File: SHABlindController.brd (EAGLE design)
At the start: 123 x 24 mm, 37 parts, among them IC1 SPARKCORE, IC2 RAC02-05SC, IC3 RXB1SIL, Q1 2N7002, Q2 2N7002

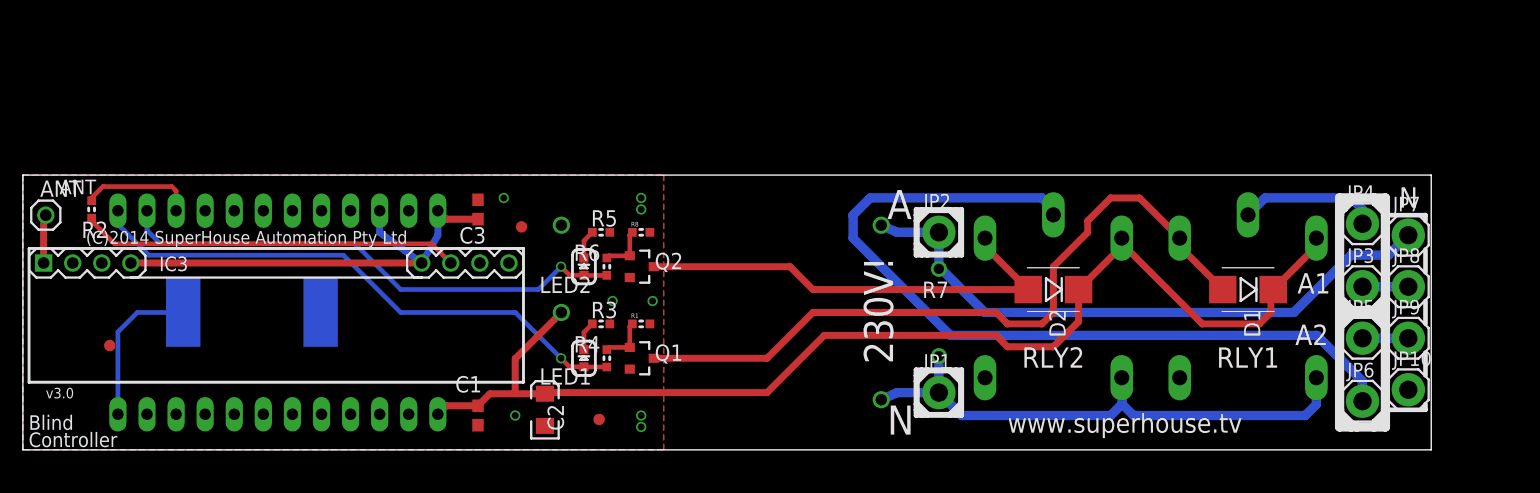
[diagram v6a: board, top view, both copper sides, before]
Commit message: v4.0 release: improved 433MHz rx footprint, added PTH option for piezo
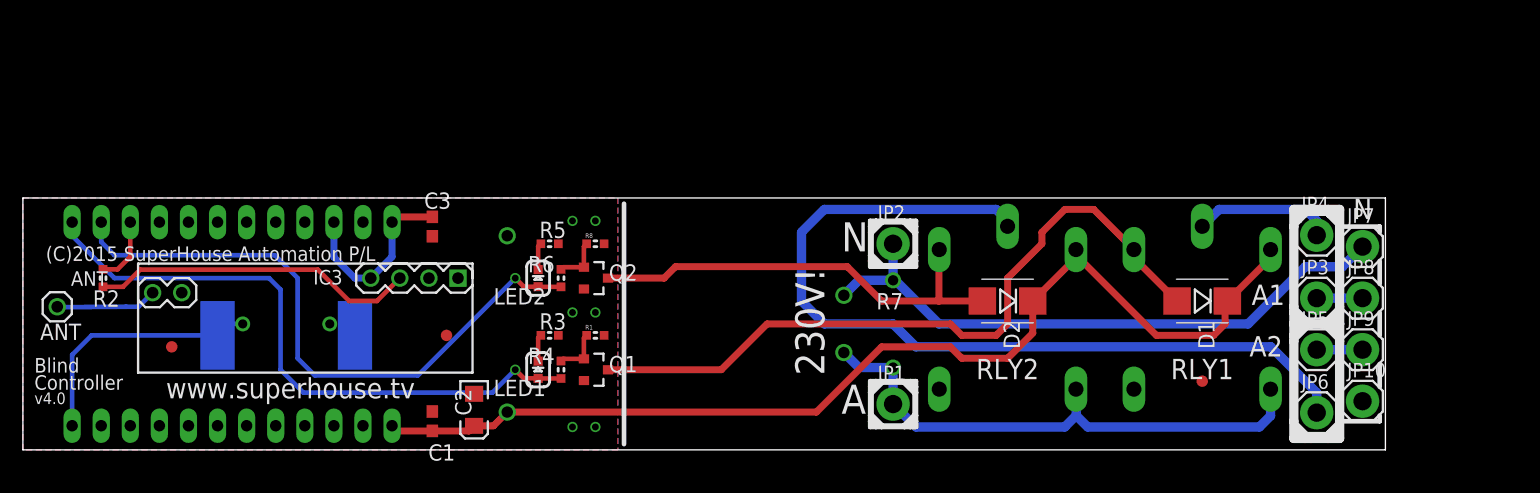
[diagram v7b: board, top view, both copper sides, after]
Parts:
- removed PIEZO: BUZZERSMD12X12, freetronics-master-v1:BUZZER-12X12-SMT
- added PIEZO1: BUZZERSMD12X12, freetronics-master-v1:BUZZER-12X12-SMT
- added PIEZO2: PIEZOPOLARISED, freetronics-jon:PIEZO12MMWIDEPOLARISED
- IC2: value RAC02-05SC -> HLKPM01; device freetronics-jon:RAC0X-SC -> freetronics-jon:HLKPM01
- IC3: value RXB1SIL -> RXB1; device PracticalArduino:RX-B1 -> freetronics-master-v1:RX-B1-SHORT-FLAT
- moved FID1 52.8 mm to (103.0, 6.00)
- moved IC3 17.2 mm to (38.0, 15.0), turned to 180 degrees
- moved FID3 11.5 mm to (37.0, 10.0)
- moved ANT 8.06 mm to (3.00, 12.5)
- moved C2 6.18 mm to (39.4, 3.50), turned to 270 degrees
- moved R2 6.08 mm to (7.00, 15.0)
- moved FID2 5.41 mm to (13.0, 9.00)
- moved R3 4.61 mm to (46.0, 10.0)
- moved R5 4.61 mm to (46.0, 18.0)
- moved C3 4.25 mm to (35.8, 19.5), turned to 270 degrees
- moved D1 4.12 mm to (103.0, 13.0)
- moved D2 4.12 mm to (86.0, 13.0)
- moved IC1 4.12 mm to (17.0, 11.0)
- moved IC2 4.12 mm to (57.0, 11.0)
- moved JP1 4.12 mm to (76.0, 4.00)
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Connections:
- net A0: now also PIEZO1.1, PIEZO2.1; no longer PIEZO.1
- net GND: now also IC3.1, IC3.5, PIEZO1.2, PIEZO2.2; no longer IC3.10, IC3.11, IC3.25, PIEZO.2
- net N$1: now also IC3.6; no longer IC3.9
- net N$135: now also IC3.3; no longer IC3.23
- net VCC: now also IC3.4; no longer IC3.12, IC3.22
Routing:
- net VCC: track 40.6 -> 16.4 mm
- net D1: track 45.2 -> 54.7 mm
- net A0: track 13.6 -> 22.4 mm
- net VIN: track 102.7 -> 94.3 mm
- net D0: track 49.1 -> 54.8 mm
- net N$1: track 4.26 -> 8.86 mm
- net N$135: track 33.1 -> 28.5 mm
- net D2: track 9.92 -> 5.85 mm
- net N$17: track 72.4 -> 75.8 mm
- net N$3: track 39.6 -> 38.9 mm
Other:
- board size 123 x 24 mm -> 119 x 22 mm
- board text added: "(C)2015 SuperHouse Automation P/L"
- board text added: "v4.0"
- board text removed: "(C)2014 SuperHouse Automation Pty Ltd"
- board text removed: "v3.0"

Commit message: v4.1 release: Added fuse mount; added Molex 15-24-4441 (8981 series) connector
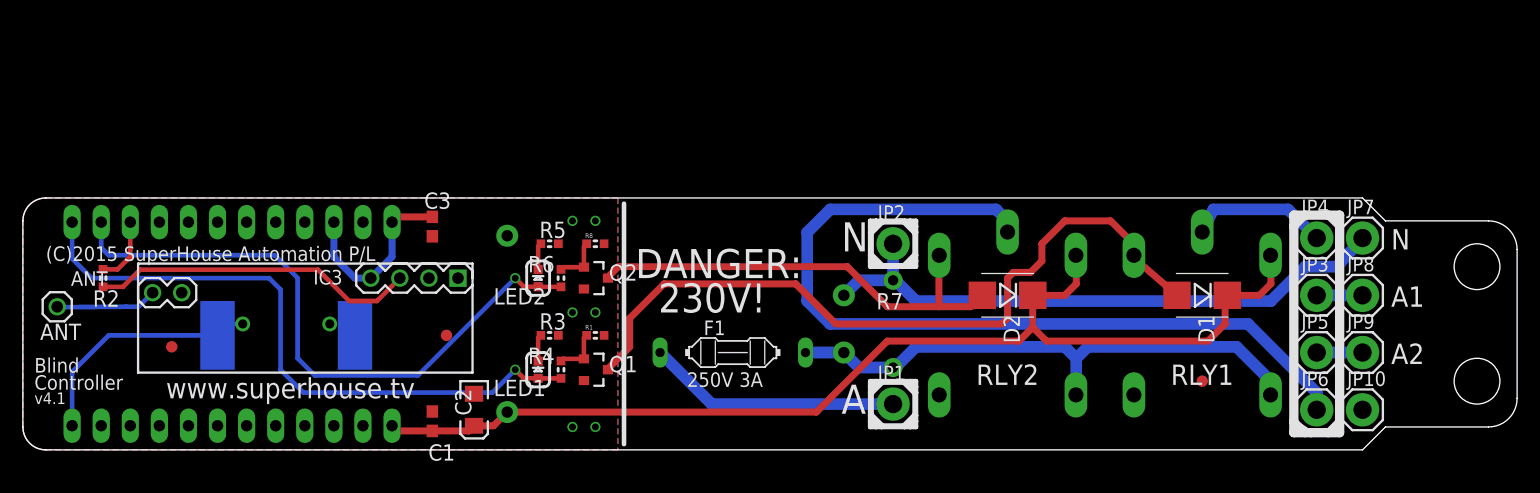
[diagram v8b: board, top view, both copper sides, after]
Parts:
- added F1: (no value), freetronics-jon:PICOFUSE
- moved JP10 0.75 mm to (117.0, 3.50)
- moved JP7 0.75 mm to (117.0, 18.5)
- moved D1 0.50 mm to (103.0, 13.5)
- moved D2 0.50 mm to (86.0, 13.5)
- moved RLY1 0.50 mm to (103.0, 9.50)
- moved RLY2 0.50 mm to (86.0, 9.50)
- moved JP3 0.25 mm to (113.0, 13.5)
- moved JP4 0.25 mm to (113.0, 18.5)
- moved JP5 0.25 mm to (113.0, 8.50)
- moved JP6 0.25 mm to (113.0, 3.50)
- moved JP8 0.25 mm to (117.0, 13.5)
- moved JP9 0.25 mm to (117.0, 8.50)
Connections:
- new net N$9: F1.1, JP1.1
- net ACTIVE: now also F1.2; no longer JP1.1
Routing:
- net N$9: track 0.00 -> 22.2 mm
- net N$4: track 63.0 -> 65.8 mm
- net VIN: track 94.3 -> 96.6 mm
- net N$3: track 38.9 -> 40.7 mm
- net NEUTRAL: track 53.7 -> 52.4 mm
- net D0: track 54.8 -> 56.0 mm
- net ACTIVE: track 47.7 -> 48.9 mm
- net A0: track 22.4 -> 21.5 mm
- net N$17: track 75.8 -> 75.0 mm
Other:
- board size 119 x 22 mm -> 130.5 x 22 mm
- board text added: "250V 3A"
- board text added: "DANGER:"
- board text added: "v4.1"
- board text removed: "v4.0"
